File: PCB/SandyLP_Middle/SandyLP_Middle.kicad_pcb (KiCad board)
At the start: 2 copper layers, 113.1 x 58.7 mm, 65 parts

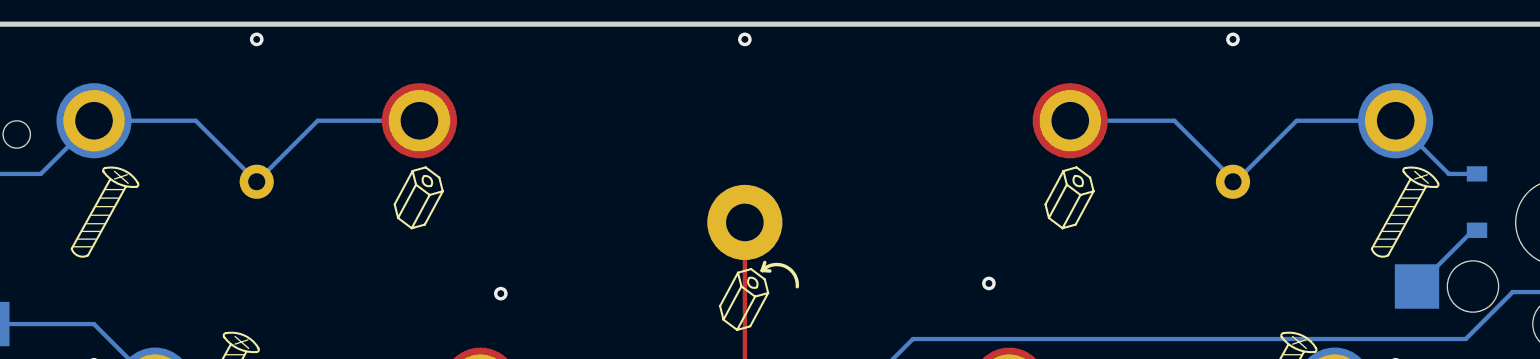
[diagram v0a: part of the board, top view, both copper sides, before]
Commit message: オプションが無料になったのでJLCのマーキングを削除。その他シルク位置調整。
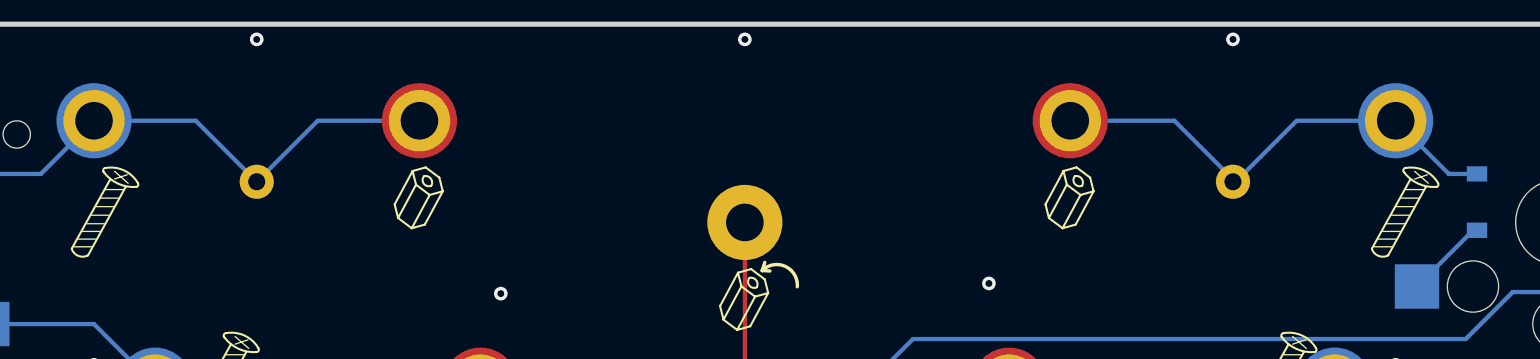
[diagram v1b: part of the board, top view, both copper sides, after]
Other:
- board text removed: "JLCJLCJLCJLC"
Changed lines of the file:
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@@
 		(fp_arc
 			(start 2.475824 -5.107131)
-			(mid 1.399999 -5.299999)
+			(mid 1.4 -5.3)
 			(end 0.555319 -5.993622)
 			(stroke
@@
 		(fp_arc
 			(start 95.805 -16.764254)
-			(mid 96.390776 -18.178462)
+			(mid 96.39077 -18.178497)
 			(end 97.805 -18.764254)
 			(stroke
@@
 		(fp_arc
 			(start 140.485 -18.764254)
-			(mid 141.899233 -18.178471)
+			(mid 141.899197 -18.178465)
 			(end 142.485 -16.764254)
 			(stroke
@@
 		(fp_arc
 			(start 142.475 -2.628468)
-			(mid 141.889208 -1.21424)
+			(mid 141.889202 -1.214275)
 			(end 140.475 -0.628468)
 			(stroke
@@
 		(fp_arc
 			(start 27.975 35.520746)
-			(mid 27.389212 36.934959)
+			(mid 27.389211 36.934956)
 			(end 25.975 37.520746)
 			(stroke
@@
 		(fp_arc
 			(start 2.475824 -5.107131)
-			(mid 1.399999 -5.299999)
+			(mid 1.4 -5.3)
 			(end 0.555319 -5.993622)
 			(stroke
@@
 		(fp_arc
 			(start 2.475824 -5.107131)
-			(mid 1.399999 -5.299999)
+			(mid 1.4 -5.3)
 			(end 0.555319 -5.993622)
 			(stroke
@@
 		(fp_arc
 			(start -1.308116 0.190917)
-			(mid 0.050001 -0.05)
+			(mid 0.05 -0.05)
 			(end 0.743353 1.142386)
 			(stroke
@@
 		(fp_arc
 			(start 2.475824 -5.107131)
-			(mid 1.399999 -5.299999)
+			(mid 1.4 -5.3)
 			(end 0.555319 -5.993622)
 			(stroke
@@
 		(fp_arc
 			(start 2.475824 -5.107131)
-			(mid 1.399999 -5.299999)
+			(mid 1.4 -5.3)
 			(end 0.555319 -5.993622)
 			(stroke
@@
 		(fp_arc
 			(start -1.308116 0.190917)
-			(mid 0.050001 -0.05)
+			(mid 0.05 -0.05)
 			(end 0.743353 1.142386)
 			(stroke
@@
 		(fp_arc
 			(start 2.475824 -5.107131)
-			(mid 1.399999 -5.299999)
+			(mid 1.4 -5.3)
 			(end 0.555319 -5.993622)
 			(stroke
@@
 		(fp_arc
 			(start 2.475824 -5.107131)
-			(mid 1.399999 -5.299999)
+			(mid 1.4 -5.3)
 			(end 0.555319 -5.993622)
 			(stroke
@@
 		(fp_arc
 			(start 2.475824 -5.107131)
-			(mid 1.399999 -5.299999)
+			(mid 1.4 -5.3)
 			(end 0.555319 -5.993622)
 			(stroke
@@
 		(fp_arc
 			(start 0.325 1.05)
-			(mid -0.050512 2.285658)
+			(mid -0.050512 2.285659)
 			(end -1.332701 2.440097)
 			(stroke
@@
 		(fp_arc
 			(start 0.325 1.05)
-			(mid -0.050512 2.285658)
+			(mid -0.050512 2.285659)
 			(end -1.332701 2.440097)
 			(stroke
@@
 		(fp_arc
 			(start 0.325 1.05)
-			(mid -0.050512 2.285658)
+			(mid -0.050512 2.285659)
 			(end -1.332701 2.440097)
 			(stroke
@@
 		(fp_arc
 			(start 0.325 1.05)
-			(mid -0.050512 2.285658)
+			(mid -0.050512 2.285659)
 			(end -1.332701 2.440097)
 			(stroke
@@
 		(fp_arc
 			(start 0.325 1.05)
-			(mid -0.050512 2.285658)
+			(mid -0.050512 2.285659)
 			(end -1.332701 2.440097)
 			(stroke
@@
 		(fp_arc
 			(start 0.325 1.05)
-			(mid -0.050512 2.285658)
+			(mid -0.050512 2.285659)
 			(end -1.332701 2.440097)
 			(stroke
@@
 		(fp_arc
 			(start 0.325 1.05)
-			(mid -0.050512 2.285658)
+			(mid -0.050512 2.285659)
 			(end -1.332701 2.440097)
 			(stroke
@@
 		(fp_arc
 			(start 0.325 1.05)
-			(mid -0.050511 2.285658)
+			(mid -0.050512 2.285658)
 			(end -1.332701 2.440097)
 			(stroke
@@
 		)
 	)
-	(gr_text "JLCJLCJLCJLC"
-		(at 218.702185 49.62528 90)
-		(layer "B.SilkS")
-		(effects
-			(font
-				(size 1.5 1.5)
-				(thickness 0.3)
-			)
-			(justify mirror)
-		)
-	)

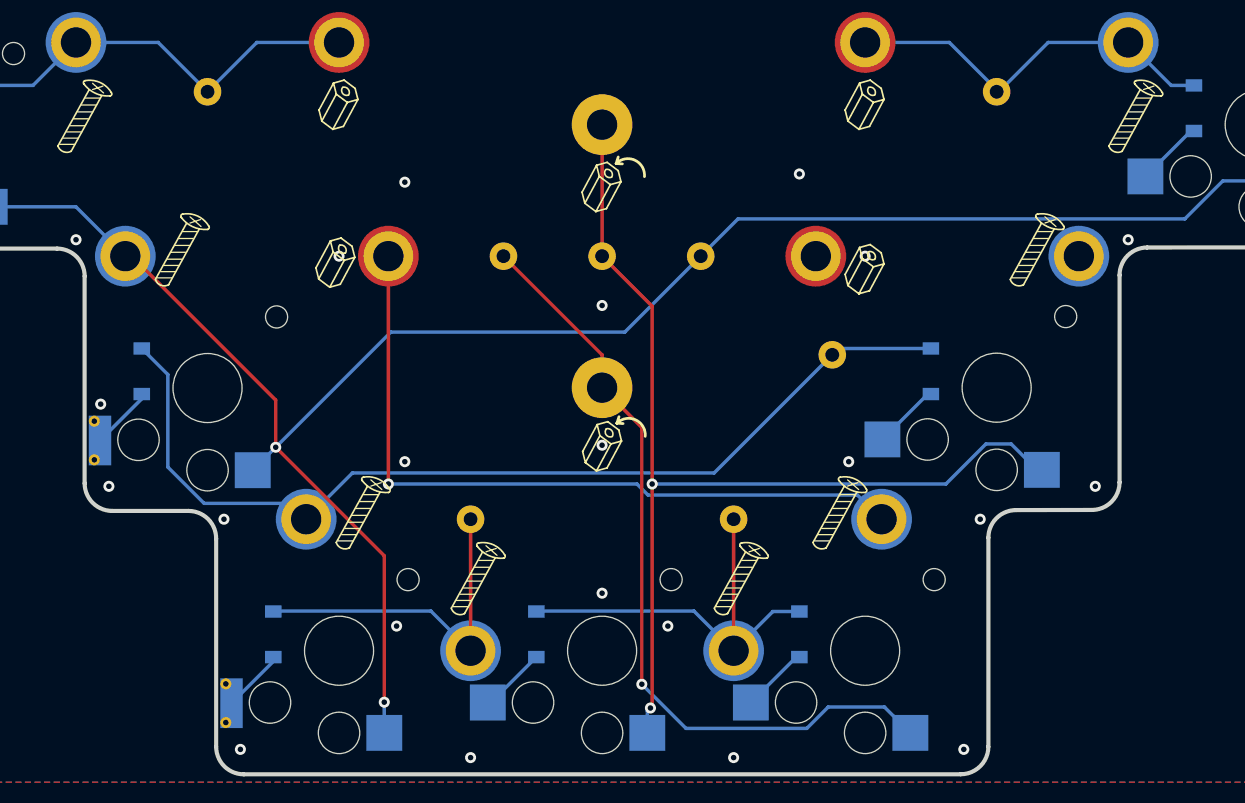
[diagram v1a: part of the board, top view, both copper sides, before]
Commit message: ネジとソケットのパッドか近くはんだ付けが心配なため、パッドを少し小さくする。
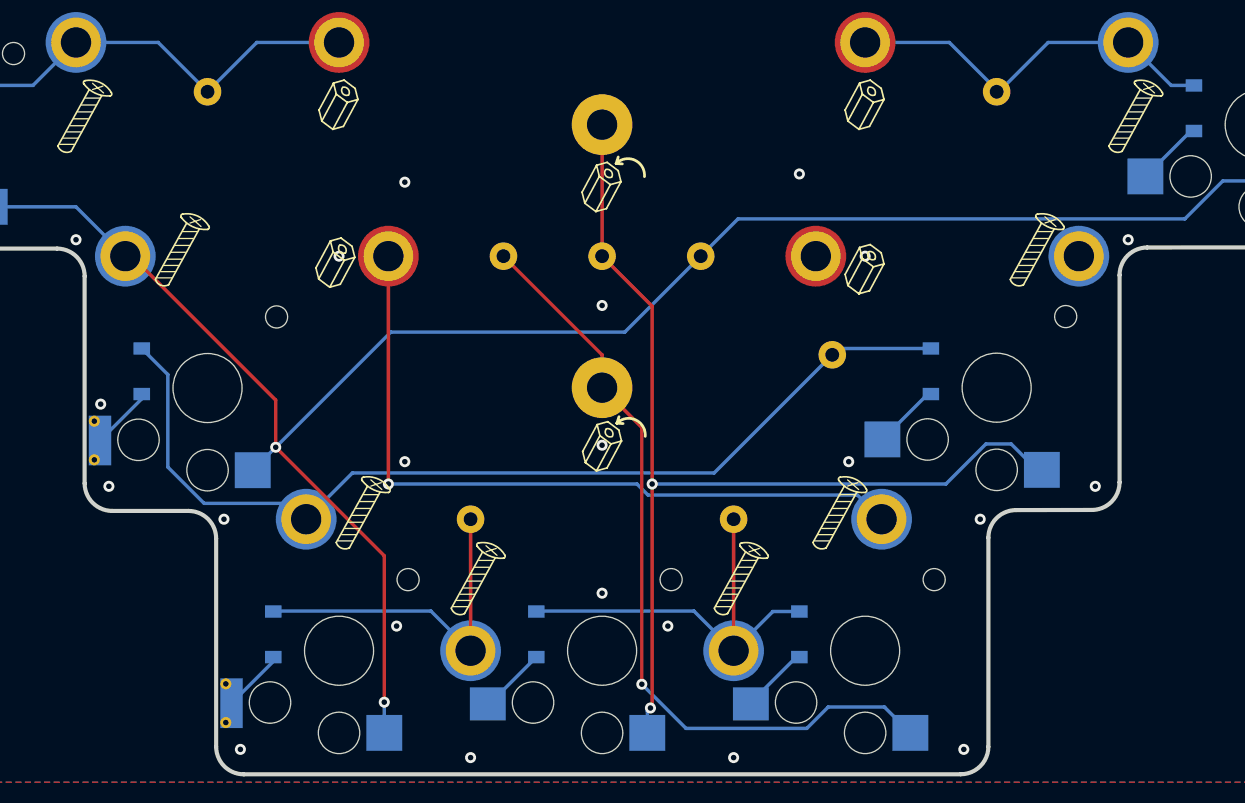
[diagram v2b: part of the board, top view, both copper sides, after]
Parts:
- SW_R4CNT_C1, SW_R4CNT_R1: footprint locallib:Kailh_socket_ChocV2 -> locallib:Kailh_socket_ChocV2_narrow_#2pad
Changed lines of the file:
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@@
 		(fp_arc
 			(start 2.475824 -5.107131)
-			(mid 1.4 -5.3)
+			(mid 1.399999 -5.299999)
 			(end 0.555319 -5.993622)
 			(stroke
@@
 		)
 	)
-	(footprint "locallib:Kailh_socket_ChocV2"
+	(footprint "locallib:Kailh_socket_ChocV2_narrow_#2pad"
 		(layer "F.Cu")
 		(at 182.983435 87.72528)
@@
 			)
 		)
-		(property "Footprint" "locallib:Kailh_socket_ChocV2"
+		(property "Footprint" "locallib:Kailh_socket_ChocV2_narrow_#2pad"
 			(at 0 0 0)
 			(layer "F.Fab")
@@
 		)
 		(pad "2" smd rect
-			(at -8.275 3.75)
-			(size 2.6 2.6)
+			(at -8.275 3.85)
+			(size 2.6 2.4)
 			(layers "B.Cu" "B.Paste" "B.Mask")
 			(net 14 "Net-(D13-A)")
@@
 		(fp_arc
 			(start 95.805 -16.764254)
-			(mid 96.39077 -18.178497)
+			(mid 96.390776 -18.178462)
 			(end 97.805 -18.764254)
 			(stroke
@@
 		(fp_arc
 			(start 140.485 -18.764254)
-			(mid 141.899197 -18.178465)
+			(mid 141.899233 -18.178471)
 			(end 142.485 -16.764254)
 			(stroke
@@
 		(fp_arc
 			(start 142.475 -2.628468)
-			(mid 141.889202 -1.214275)
+			(mid 141.889208 -1.21424)
 			(end 140.475 -0.628468)
 			(stroke
@@
 		(fp_arc
 			(start 27.975 35.520746)
-			(mid 27.389211 36.934956)
+			(mid 27.389212 36.934959)
 			(end 25.975 37.520746)
 			(stroke
@@
 		(fp_arc
 			(start 2.475824 -5.107131)
-			(mid 1.4 -5.3)
+			(mid 1.399999 -5.299999)
 			(end 0.555319 -5.993622)
 			(stroke
@@
 		(fp_arc
 			(start 2.475824 -5.107131)
-			(mid 1.4 -5.3)
+			(mid 1.399999 -5.299999)
 			(end 0.555319 -5.993622)
 			(stroke
@@
 		(fp_arc
 			(start -1.308116 0.190917)
-			(mid 0.05 -0.05)
+			(mid 0.050001 -0.05)
 			(end 0.743353 1.142386)
 			(stroke
@@
 		(fp_arc
 			(start 2.475824 -5.107131)
-			(mid 1.4 -5.3)
+			(mid 1.399999 -5.299999)
 			(end 0.555319 -5.993622)
 			(stroke
@@
 		)
 	)
-	(footprint "locallib:Kailh_socket_ChocV2"
+	(footprint "locallib:Kailh_socket_ChocV2_narrow_#2pad"
 		(layer "F.Cu")
 		(at 163.933435 87.72528)
@@
 			)
 		)
-		(property "Footprint" "locallib:Kailh_socket_ChocV2"
+		(property "Footprint" "locallib:Kailh_socket_ChocV2_narrow_#2pad"
 			(at 0 0 0)
 			(layer "F.Fab")
@@
 			(layer "F.Fab")
 		)
-		(fp_text user "${REFERENCE}"
-			(at -3 5 0)
+		(fp_text user "${VALUE}"
+			(at -1 9 0)
 			(layer "B.Fab")
 			(effects
@@
 			)
 		)
-		(fp_text user "${VALUE}"
-			(at -1 9 0)
+		(fp_text user "${REFERENCE}"
+			(at -3 5 0)
 			(layer "B.Fab")
 			(effects
@@
 		)
 		(pad "2" smd rect
-			(at -8.275 3.75)
-			(size 2.6 2.6)
+			(at -8.275 3.85)
+			(size 2.6 2.4)
 			(layers "B.Cu" "B.Paste" "B.Mask")
 			(net 13 "Net-(D12-A)")
@@
 		(fp_arc
 			(start 2.475824 -5.107131)
-			(mid 1.4 -5.3)
+			(mid 1.399999 -5.299999)
 			(end 0.555319 -5.993622)
 			(stroke
@@
 		(fp_arc
 			(start -1.308116 0.190917)
-			(mid 0.05 -0.05)
+			(mid 0.050001 -0.05)
 			(end 0.743353 1.142386)
 			(stroke
@@
 		(fp_arc
 			(start 2.475824 -5.107131)
-			(mid 1.4 -5.3)
+			(mid 1.399999 -5.299999)
 			(end 0.555319 -5.993622)
 			(stroke
@@
 		(fp_arc
 			(start 2.475824 -5.107131)
-			(mid 1.4 -5.3)
+			(mid 1.399999 -5.299999)
 			(end 0.555319 -5.993622)
 			(stroke
@@
 		(fp_arc
 			(start 2.475824 -5.107131)
-			(mid 1.4 -5.3)
+			(mid 1.399999 -5.299999)
 			(end 0.555319 -5.993622)
 			(stroke
@@
 		(fp_arc
 			(start 0.325 1.05)
-			(mid -0.050512 2.285659)
+			(mid -0.050511 2.285659)
 			(end -1.332701 2.440097)
 			(stroke
@@
 		(fp_arc
 			(start 0.325 1.05)
-			(mid -0.050512 2.285659)
+			(mid -0.050511 2.285659)
 			(end -1.332701 2.440097)
 			(stroke
@@
 		(fp_arc
 			(start 0.325 1.05)
-			(mid -0.050512 2.285659)
+			(mid -0.050511 2.285659)
 			(end -1.332701 2.440097)
 			(stroke
@@
 		(fp_arc
 			(start 0.325 1.05)
-			(mid -0.050512 2.285659)
+			(mid -0.050511 2.285659)
 			(end -1.332701 2.440097)
 			(stroke
@@
 		(fp_arc
 			(start 0.325 1.05)
-			(mid -0.050512 2.285659)
+			(mid -0.050511 2.285659)
 			(end -1.332701 2.440097)
 			(stroke
@@
 		(fp_arc
 			(start 0.325 1.05)
-			(mid -0.050512 2.285659)
+			(mid -0.050511 2.285659)
 			(end -1.332701 2.440097)
 			(stroke
@@
 		(fp_arc
 			(start 0.325 1.05)
-			(mid -0.050512 2.285659)
+			(mid -0.050511 2.285659)
 			(end -1.332701 2.440097)
 			(stroke
@@
 		(fp_arc
 			(start 0.325 1.05)
-			(mid -0.050512 2.285658)
+			(mid -0.050512 2.285659)
 			(end -1.332701 2.440097)
 			(stroke

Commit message: Mid基板　ゴムシート貼り付け指標
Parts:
- moved REF** 7.98 mm to (168.4, 92.4)
- moved REF** 7.95 mm to (149.4, 92.4)
- moved REF** 6.84 mm to (170.4, 86.9)
- moved REF** 6.73 mm to (151.4, 86.9)
- moved REF** 0.83 mm to (133.4, 56.6)
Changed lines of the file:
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@@
 		(locked yes)
 		(layer "F.Cu")
-		(at 154.321126 86.132889)
+		(at 149.409345 92.387032)
 		(property "Reference" "REF**"
 			(at 0 0.5 0)
@@
 		(fp_arc
 			(start 2.475824 -5.107131)
-			(mid 1.399999 -5.299999)
+			(mid 1.4 -5.3)
 			(end 0.555319 -5.993622)
 			(stroke
@@
 		(fp_arc
 			(start 95.805 -16.764254)
-			(mid 96.390776 -18.178462)
+			(mid 96.39077 -18.178497)
 			(end 97.805 -18.764254)
 			(stroke
@@
 		(fp_arc
 			(start 140.485 -18.764254)
-			(mid 141.899233 -18.178471)
+			(mid 141.899197 -18.178465)
 			(end 142.485 -16.764254)
 			(stroke
@@
 		(fp_arc
 			(start 142.475 -2.628468)
-			(mid 141.889208 -1.21424)
+			(mid 141.889202 -1.214275)
 			(end 140.475 -0.628468)
 			(stroke
@@
 		(fp_arc
 			(start 27.975 35.520746)
-			(mid 27.389212 36.934959)
+			(mid 27.389211 36.934956)
 			(end 25.975 37.520746)
 			(stroke
@@
 		(fp_arc
 			(start 2.475824 -5.107131)
-			(mid 1.399999 -5.299999)
+			(mid 1.4 -5.3)
 			(end 0.555319 -5.993622)
 			(stroke
@@
 		(locked yes)
 		(layer "F.Cu")
-		(at 173.371126 86.132889)
+		(at 168.409345 92.387032)
 		(property "Reference" "REF**"
 			(at 0 0.5 0)
@@
 		(fp_arc
 			(start 2.475824 -5.107131)
-			(mid 1.399999 -5.299999)
+			(mid 1.4 -5.3)
 			(end 0.555319 -5.993622)
 			(stroke
@@
 		(fp_arc
 			(start -1.308116 0.190917)
-			(mid 0.050001 -0.05)
+			(mid 0.05 -0.05)
 			(end 0.743353 1.142386)
 			(stroke
@@
 		(fp_arc
 			(start 2.475824 -5.107131)
-			(mid 1.399999 -5.299999)
+			(mid 1.4 -5.3)
 			(end 0.555319 -5.993622)
 			(stroke
@@
 		(fp_arc
 			(start 2.475824 -5.107131)
-			(mid 1.399999 -5.299999)
+			(mid 1.4 -5.3)
 			(end 0.555319 -5.993622)
 			(stroke
@@
 		(fp_arc
 			(start -1.308116 0.190917)
-			(mid 0.050001 -0.05)
+			(mid 0.05 -0.05)
 			(end 0.743353 1.142386)
 			(stroke
@@
 		(fp_arc
 			(start 2.475824 -5.107131)
-			(mid 1.399999 -5.299999)
+			(mid 1.4 -5.3)
 			(end 0.555319 -5.993622)
 			(stroke
@@
 		(fp_arc
 			(start 2.475824 -5.107131)
-			(mid 1.399999 -5.299999)
+			(mid 1.4 -5.3)
 			(end 0.555319 -5.993622)
 			(stroke
@@
 		(fp_arc
 			(start 2.475824 -5.107131)
-			(mid 1.399999 -5.299999)
+			(mid 1.4 -5.3)
 			(end 0.555319 -5.993622)
 			(stroke
@@
 		(locked yes)
 		(layer "B.Cu")
-		(at 133.085027 55.8479)
+		(at 133.428777 56.607275)
 		(property "Reference" "REF**"
 			(at 0 -0.5 0)
@@
 		(fp_arc
 			(start 0.325 1.05)
-			(mid -0.050511 2.285659)
+			(mid -0.050511 2.285658)
 			(end -1.332701 2.440097)
 			(stroke
@@
 		(fp_arc
 			(start 0.325 1.05)
-			(mid -0.050511 2.285659)
+			(mid -0.050511 2.285658)
 			(end -1.332701 2.440097)
 			(stroke
@@
 		(tags "test point THT pad")
 		(property "Reference" "EXT_MR6"
-			(at 0 1.998 0)
+			(at 4.8125 -0.08125 0)
 			(layer "B.SilkS")
 			(effects
@@
 		(fp_arc
 			(start 0.325 1.05)
-			(mid -0.050511 2.285659)
+			(mid -0.050511 2.285658)
 			(end -1.332701 2.440097)
 			(stroke
@@
 		(fp_arc
 			(start 0.325 1.05)
-			(mid -0.050511 2.285659)
+			(mid -0.050511 2.285658)
 			(end -1.332701 2.440097)
 			(stroke
@@
 		(locked yes)
 		(layer "B.Cu")
-		(at 154.321126 80.851025)
+		(at 151.378777 86.907275)
 		(property "Reference" "REF**"
 			(at 0 -0.5 0)
@@
 		(fp_arc
 			(start 0.325 1.05)
-			(mid -0.050511 2.285659)
+			(mid -0.050511 2.285658)
 			(end -1.332701 2.440097)
 			(stroke
@@
 		(tags "test point THT pad")
 		(property "Reference" "EXT_MR5"
-			(at 0 1.998 0)
+			(at -4.78125 0.025 0)
 			(layer "B.SilkS")
 			(effects
@@
 		(locked yes)
 		(layer "B.Cu")
-		(at 173.566277 80.851025)
+		(at 170.378777 86.907275)
 		(property "Reference" "REF**"
 			(at 0 -0.5 0)
@@
 		(fp_arc
 			(start 0.325 1.05)
-			(mid -0.050511 2.285659)
+			(mid -0.050511 2.285658)
 			(end -1.332701 2.440097)
 			(stroke
@@
 		(fp_arc
 			(start 0.325 1.05)
-			(mid -0.050511 2.285659)
+			(mid -0.050511 2.285658)
 			(end -1.332701 2.440097)
 			(stroke
@@
 		(tags "test point THT pad")
 		(property "Reference" "EXT_MR2"
-			(at 0 1.998 0)
+			(at -4.7375 0.01875 0)
 			(layer "B.SilkS")
 			(effects
@@
 		(fp_arc
 			(start 0.325 1.05)
-			(mid -0.050512 2.285659)
+			(mid -0.050511 2.285659)
 			(end -1.332701 2.440097)
 			(stroke
@@
 		)
 	)
+	(gr_line
+		(start 172.370935 69.51903)
+		(end 172.320935 76.91903)
+		(stroke
+			(width 0.5)
+			(type default)
+		)
+		(layer "B.SilkS")
+	)
+	(gr_rect
+		(start 125.320935 52.21903)
+		(end 201.570935 56.46903)
+		(stroke
+			(width 0.5)
+			(type default)
+		)
+		(fill none)
+		(layer "B.SilkS")
+	)
+	(gr_line
+		(start 176.620935 69.51903)
+		(end 172.370935 69.51903)
+		(stroke
+			(width 0.5)
+			(type default)
+		)
+		(layer "B.SilkS")
+	)
+	(gr_rect
+		(start 216.570935 45.71903)
+		(end 219.820935 57.21903)
+		(stroke
+			(width 0.5)
+			(type default)
+		)
+		(fill none)
+		(layer "B.SilkS")
+	)
+	(gr_rect
+		(start 168.995935 64.46903)
+		(end 182.445935 68.71903)
+		(stroke
+			(width 0.5)
+			(type default)
+		)
+		(fill none)
+		(layer "B.SilkS")
+	)
+	(gr_line
+		(start 176.620935 84.76903)
+		(end 176.620935 69.51903)
+		(stroke
+			(width 0.5)
+			(type default)
+		)
+		(layer "B.SilkS")
+	)
+	(gr_rect
+		(start 144.620935 64.46903)
+		(end 158.070935 68.71903)
+		(stroke
+			(width 0.5)
+			(type default)
+		)
+		(fill none)
+		(layer "B.SilkS")
+	)
+	(gr_line
+		(start 172.370935 79.51903)
+		(end 172.370935 84.76903)
+		(stroke
+			(width 0.5)
+			(type default)
+		)
+		(layer "B.SilkS")
+	)
+	(gr_rect
+		(start 116.220935 39.11903)
+		(end 123.070935 43.36903)
+		(stroke
+			(width 0.5)
+			(type default)
+		)
+		(fill none)
+		(layer "B.SilkS")
+	)
+	(gr_line
+		(start 172.370935 84.76903)
+		(end 176.620935 84.76903)
+		(stroke
+			(width 0.5)
+			(type default)
+		)
+		(layer "B.SilkS")
+	)
+	(gr_rect
+		(start 148.420935 69.46903)
+		(end 152.670935 84.71903)
+		(stroke
+			(width 0.5)
+			(type default)
+		)
+		(fill none)
+		(layer "B.SilkS")
+	)
+	(gr_rect
+		(start 147.570935 39.21903)
+		(end 180.320935 43.96903)
+		(stroke
+			(width 0.5)
+			(type default)
+		)
+		(fill none)
+		(layer "B.SilkS")
+	)
 	(gr_text "Back Side"
-		(at 163.933435 44.86278 0)
+		(at 163.933435 41.71903 0)
 		(layer "B.SilkS" knockout)
 		(effects
@@
 		)
 	)
-	(gr_text "#SandyLP_kbd DN0010\nMid by @jpskenn"
-		(at 179.41156 73.85028 0)
+	(gr_text "#SandyLP_kbd DN0010 Mid by @jpskenn"
+		(at 163.920935 54.41903 0)
 		(layer "B.SilkS")
 		(effects
@@
 				(thickness 0.2)
 			)
-			(justify left mirror)
+			(justify mirror)
 		)
 	)
